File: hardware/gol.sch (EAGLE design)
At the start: 40 parts, among them U1 STM32F072CBT

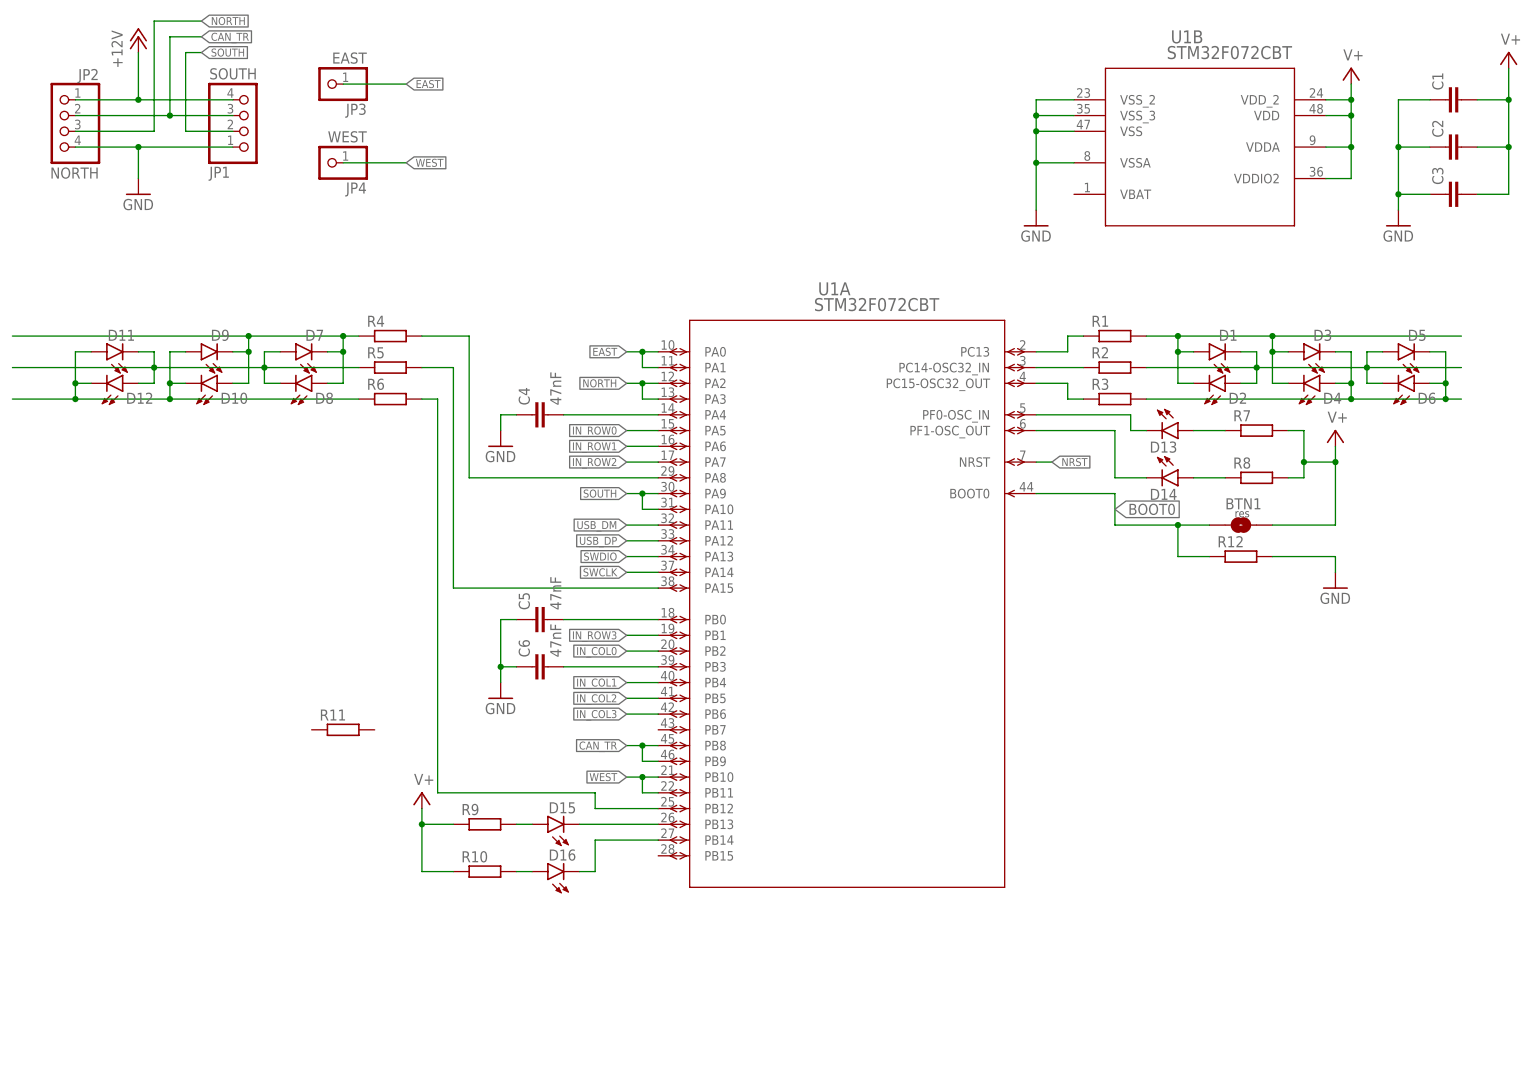
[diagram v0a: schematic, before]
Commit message: Adds buttons and LEDs, adds schematic for grids.
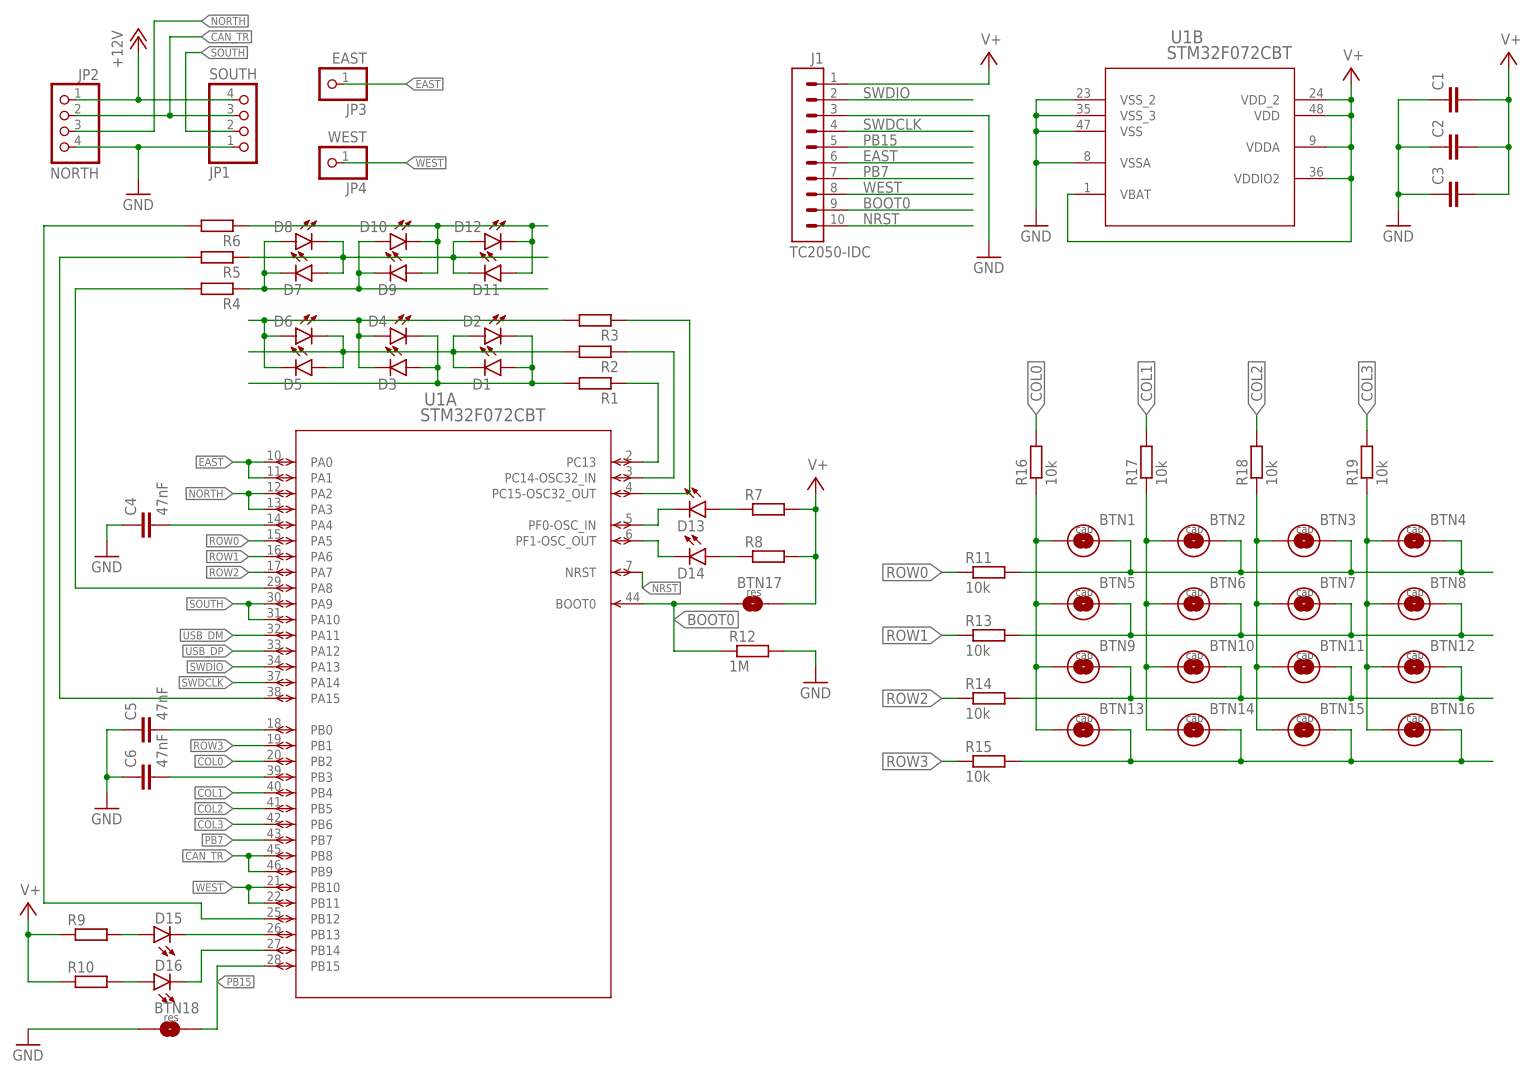
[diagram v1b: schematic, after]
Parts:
- added BTN10, BTN11, BTN12, BTN13, BTN14, BTN15, BTN16, BTN2, BTN3, BTN4, BTN5, BTN6, BTN7, BTN8, BTN9: BUTTON-CAP, parts:BUTTON-CAP
- added BTN17, BTN18: BUTTON-RES, parts:BUTTON-RES
- added J1: TC2050-IDC, tcs:TC2050-IDC
- added R13, R14, R15, R16, R17, R18, R19: 10k, rcl:R-EU_R0603
- BTN1: value BUTTON-RES -> BUTTON-CAP; device parts:BUTTON-RES -> parts:BUTTON-CAP
- R11: value (none) -> 10k; device rcl:R-EU_0207/10 -> rcl:R-EU_R0603
- R12: value (none) -> 1M
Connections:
- removed net SWCLK: U1A.PA14
- new net COL0: R16.2, U1A.PB2
- new net COL1: R17.2, U1A.PB4
- new net COL2: R18.2, U1A.PB5
- new net COL3: R19.2, U1A.PB6
- new net PB15: BTN18.2, J1.5, U1A.PB15
- new net PB7: J1.7, U1A.PB7
- new net ROW0: R11.1, U1A.PA5
- new net ROW1: R13.1, U1A.PA6
- new net ROW2: R14.1, U1A.PA7
- new net ROW3: R15.1, U1A.PB1
- new net SWDCLK: J1.4, U1A.PA14
- net BOOT0: now also BTN17.1, J1.9; no longer BTN1.1
- net EAST: now also J1.6
- net GND: now also BTN18.1, J1.3
- net IN_COL0: now also BTN1.1, BTN13.1, BTN5.1, BTN9.1, R16.1; no longer U1A.PB2
- net IN_COL1: now also BTN10.1, BTN14.1, BTN2.1, BTN6.1, R17.1; no longer U1A.PB4
- net IN_COL2: now also BTN11.1, BTN15.1, BTN3.1, BTN7.1, R18.1; no longer U1A.PB5
- net IN_COL3: now also BTN12.1, BTN16.1, BTN4.1, BTN8.1, R19.1; no longer U1A.PB6
- net IN_ROW0: now also BTN1.2, BTN2.2, BTN3.2, BTN4.2, R11.2; no longer U1A.PA5
- net IN_ROW1: now also BTN5.2, BTN6.2, BTN7.2, BTN8.2, R13.2; no longer U1A.PA6
- net IN_ROW2: now also BTN10.2, BTN11.2, BTN12.2, BTN9.2, R14.2; no longer U1A.PA7
- net IN_ROW3: now also BTN13.2, BTN14.2, BTN15.2, BTN16.2, R15.2; no longer U1A.PB1
- net NRST: now also J1.10
- net SWDIO: now also J1.2
- net V+: now also BTN17.2, J1.1, U1B.VBAT; no longer BTN1.2
- net WEST: now also J1.8
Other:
- moved on the sheet: C4, C5, C6, D1, D10, D11, D12, D13, D14, D15, D16, D2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

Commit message: Adds micro-usb connector and 5V to 3V3 voltage regulator.
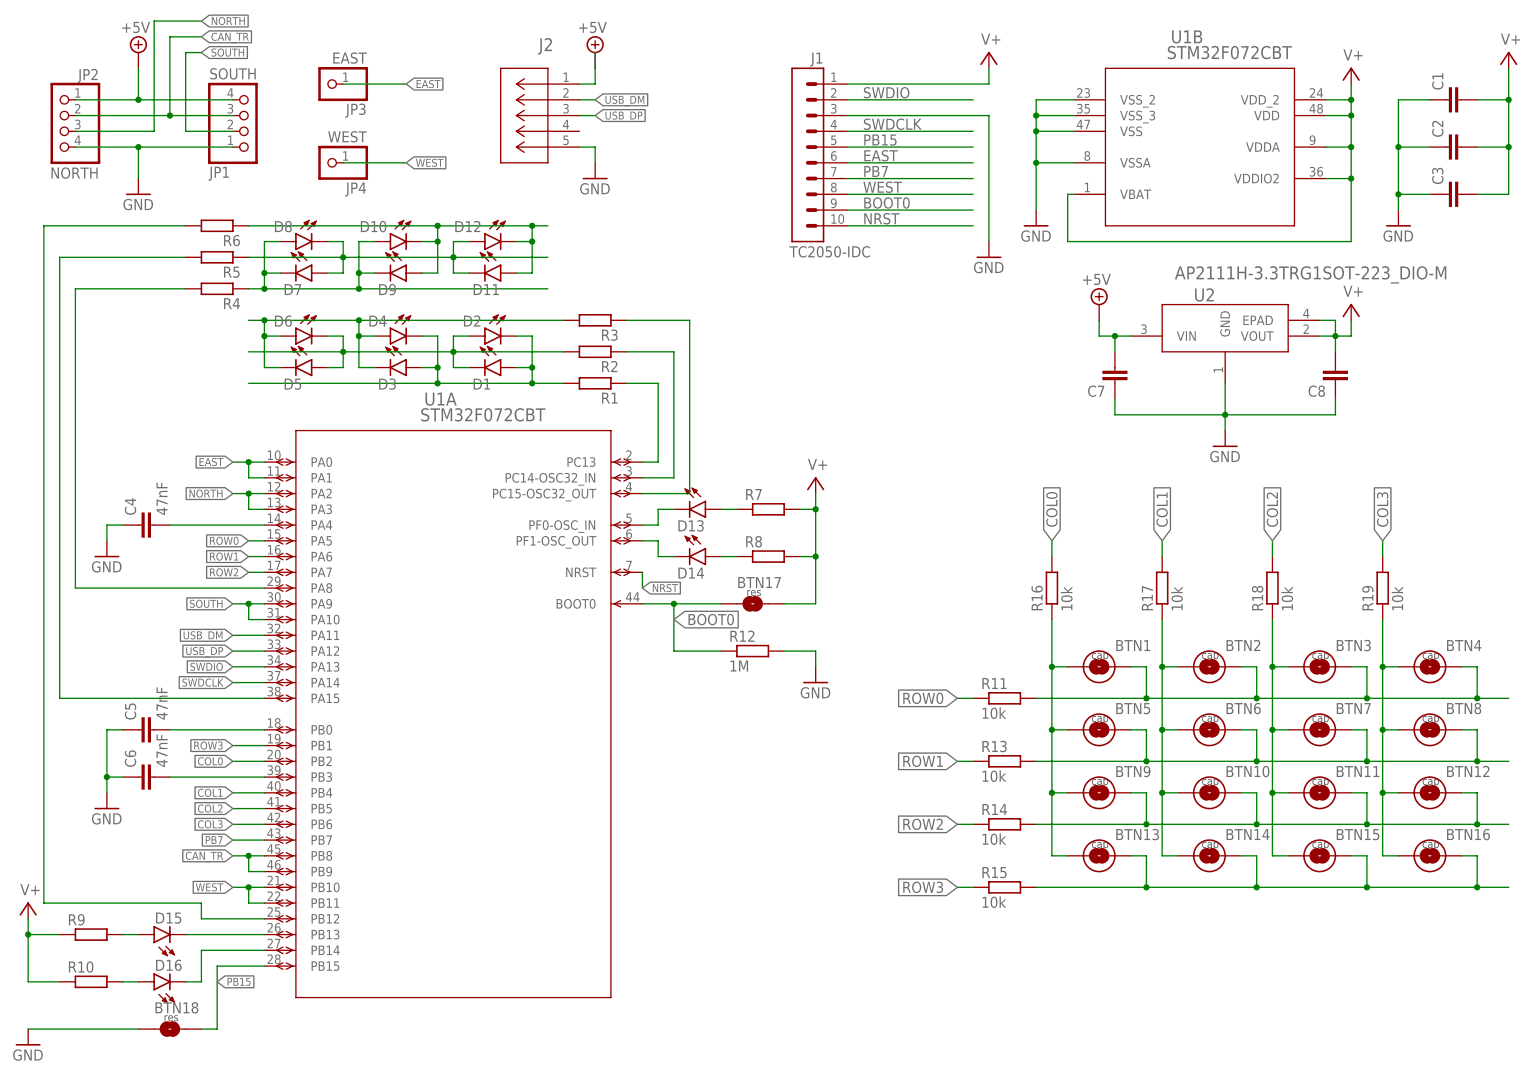
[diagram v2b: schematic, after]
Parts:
- added C7, C8: (no value), rcl:C-EUC0603
- added J2: 2057-MCR-B-S-RA-TSMT-NP-CS4-T/RCT-ND, parts:10118192-0002LFCONN_10118192-0002LF_AMP
- added U2: AP2111H-3.3TRG1SOT-223_DIO-M, parts:AP2111H-3.3TRG1SOT-223_DIO-M
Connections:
- removed net +12V: JP1.4, JP2.1
- new net +5V: C7.2, J2.1, JP1.4, JP2.1, U2.VIN
- net GND: now also C7.1, C8.1, J2.5, U2.GND
- net USB_DM: now also J2.2
- net USB_DP: now also J2.3
- net V+: now also C8.2, U2.EPAD, U2.VOUT
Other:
- moved on the sheet: BTN1, BTN10, BTN11, BTN12, BTN13, BTN14, BTN15, BTN16, BTN2, BTN3, BTN4, BTN5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

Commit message: Completes layout of top side components. Adds +12V grid horizontally.
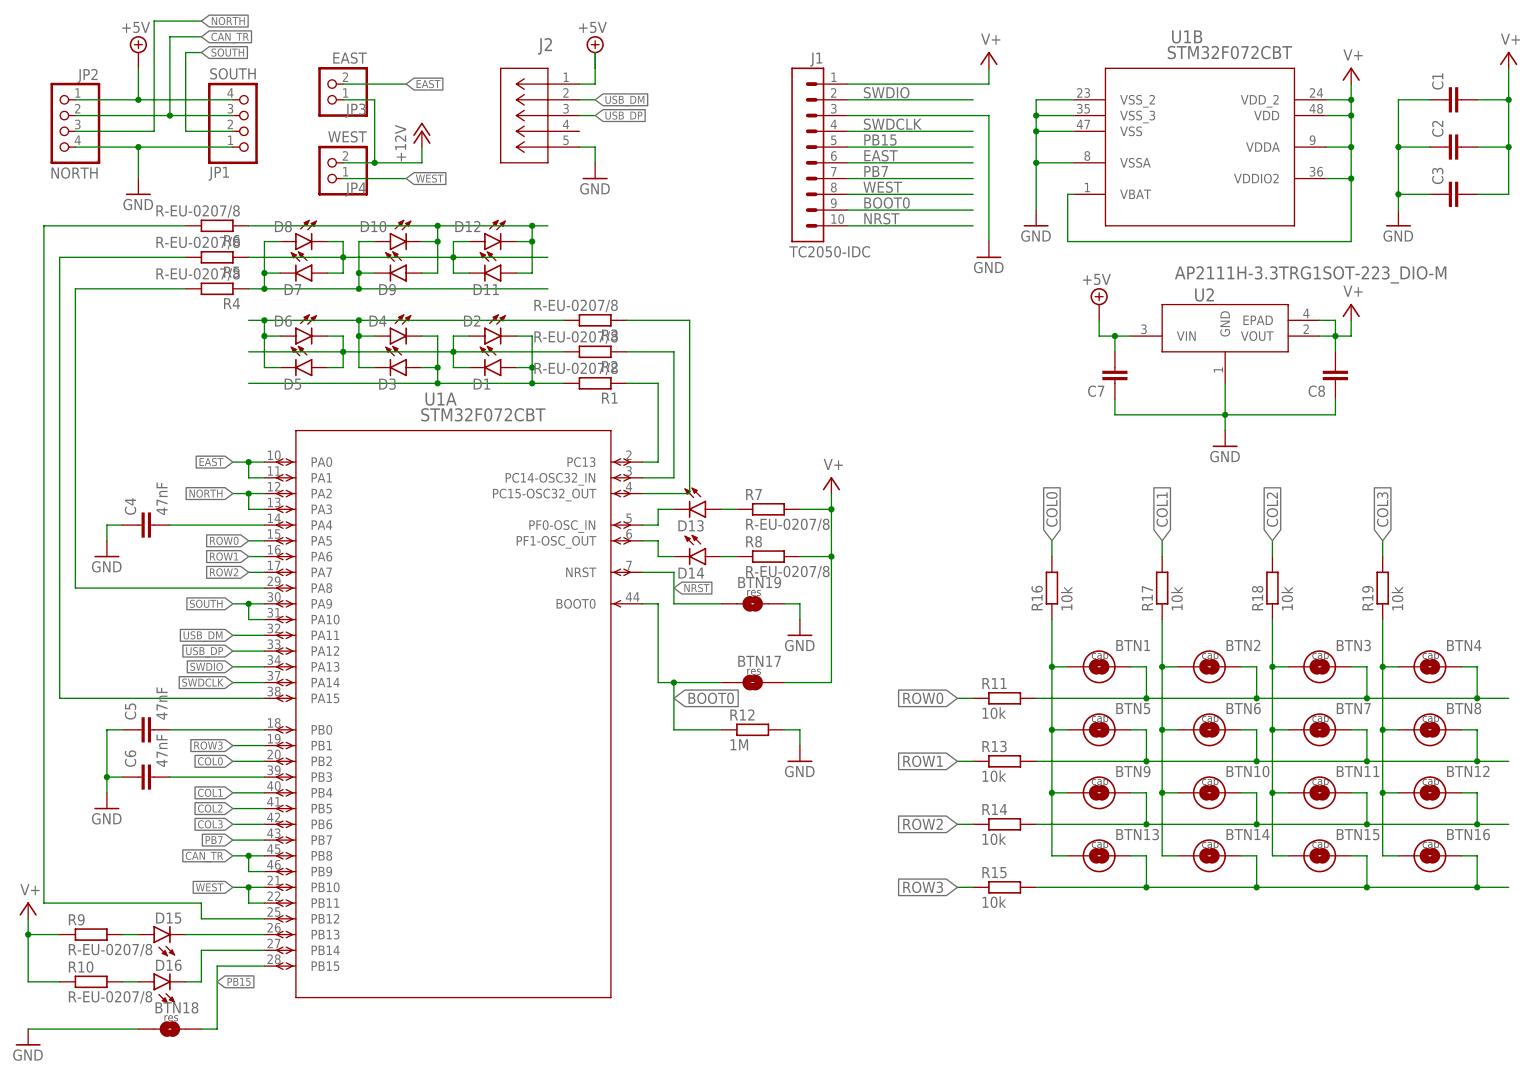
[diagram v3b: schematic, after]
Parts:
- added BTN19: RESET, parts:BUTTON-RES
- BTN17: value BUTTON-RES -> BOOT
- BTN18: value BUTTON-RES -> MENU
- JP3, JP4: device pinhead:PINHD-1X1 -> parts:PINHD-1X2
- R1, R10, R2, R3, R4, R5, R6, R7, R8, R9: value (none) -> R-EU-0207/8; device rcl:R-EU_0207/10 -> parts:R-EU-0207/8
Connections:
- new net +12V: JP3.1, JP4.2
- net EAST: now also JP3.2; no longer JP3.1
- net GND: now also BTN19.2
- net NRST: now also BTN19.1
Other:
- moved on the sheet: BTN17, R12

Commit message: Completes part of the layout and a small part of the routing around the MCU.
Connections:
- net N$10 renamed OUTB-L1
- net N$11 renamed OUTB-L2
- net N$12 renamed OUTB-L3
- net N$16 renamed OUTD13
- net N$17 renamed OUTD14
- net N$20 renamed OUTD15
- net N$21 renamed OUTD16
- net N$7 renamed OUTA-L2
- net N$8 renamed OUTA-L1
- net N$9 renamed OUTA-L3
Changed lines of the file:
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@@
 <instance part="R1" gate="G$1" x="99.06" y="114.3" smashed="yes" rot="R180">
 <attribute name="NAME" x="102.87" y="112.8014" size="1.778" layer="95" rot="R180"/>
-<attribute name="VALUE" x="102.87" y="117.602" size="1.778" layer="96" rot="R180"/>
 </instance>
 <instance part="R2" gate="G$1" x="99.06" y="119.38" smashed="yes" rot="R180">
 <attribute name="NAME" x="102.87" y="117.8814" size="1.778" layer="95" rot="R180"/>
-<attribute name="VALUE" x="102.87" y="122.682" size="1.778" layer="96" rot="R180"/>
 </instance>
 <instance part="R3" gate="G$1" x="99.06" y="124.46" smashed="yes" rot="R180">
 <attribute name="NAME" x="102.87" y="122.9614" size="1.778" layer="95" rot="R180"/>
-<attribute name="VALUE" x="102.87" y="127.762" size="1.778" layer="96" rot="R180"/>
 </instance>
 <instance part="R4" gate="G$1" x="38.1" y="129.54" smashed="yes" rot="R180">
 <attribute name="NAME" x="41.91" y="128.0414" size="1.778" layer="95" rot="R180"/>
-<attribute name="VALUE" x="41.91" y="132.842" size="1.778" layer="96" rot="R180"/>
 </instance>
 <instance part="R5" gate="G$1" x="38.1" y="134.62" smashed="yes" rot="R180">
 <attribute name="NAME" x="41.91" y="133.1214" size="1.778" layer="95" rot="R180"/>
-<attribute name="VALUE" x="41.91" y="137.922" size="1.778" layer="96" rot="R180"/>
 </instance>
 <instance part="R6" gate="G$1" x="38.1" y="139.7" smashed="yes" rot="R180">
 <attribute name="NAME" x="41.91" y="138.2014" size="1.778" layer="95" rot="R180"/>
-<attribute name="VALUE" x="41.91" y="143.002" size="1.778" layer="96" rot="R180"/>
 </instance>
 <instance part="R7" gate="G$1" x="127" y="93.98" smashed="yes">
@@
 <instance part="R9" gate="G$1" x="17.78" y="25.4" smashed="yes">
 <attribute name="NAME" x="13.97" y="26.8986" size="1.778" layer="95"/>
-<attribute name="VALUE" x="13.97" y="22.098" size="1.778" layer="96"/>
 </instance>
 <instance part="R10" gate="G$1" x="17.78" y="17.78" smashed="yes">
 <attribute name="NAME" x="13.97" y="19.2786" size="1.778" layer="95"/>
-<attribute name="VALUE" x="13.97" y="14.478" size="1.778" layer="96"/>
 </instance>
 <instance part="JP1" gate="A" x="43.18" y="157.48" smashed="yes" rot="MR180">
@@
 </segment>
 </net>
-<net name="N$7" class="0">
+<net name="OUTA-L2" class="0">
 <segment>
 <pinref part="R2" gate="G$1" pin="1"/>
@@
 </segment>
 </net>
-<net name="N$9" class="0">
+<net name="OUTA-L3" class="0">
 <segment>
 <pinref part="U1" gate="A" pin="PC15-OSC32_OUT"/>
@@
 </segment>
 </net>
-<net name="N$8" class="0">
+<net name="OUTA-L1" class="0">
 <segment>
 <pinref part="U1" gate="A" pin="PC13"/>
@@
 </segment>
 </net>
-<net name="N$10" class="0">
+<net name="OUTB-L1" class="0">
 <segment>
 <pinref part="U1" gate="A" pin="PA8"/>
@@
 </segment>
 </net>
-<net name="N$11" class="0">
+<net name="OUTB-L2" class="0">
 <segment>
 <pinref part="U1" gate="A" pin="PA15"/>
@@
 </segment>
 </net>
-<net name="N$12" class="0">
+<net name="OUTB-L3" class="0">
 <segment>
 <pinref part="R6" gate="G$1" pin="2"/>
@@
 </segment>
 </net>
-<net name="N$20" class="0">
+<net name="OUTD15" class="0">
 <segment>
 <pinref part="U1" gate="A" pin="PB13"/>
@@
 </segment>
 </net>
-<net name="N$21" class="0">
+<net name="OUTD16" class="0">
 <segment>
 <pinref part="U1" gate="A" pin="PB14"/>
@@
 </segment>
 </net>
-<net name="N$16" class="0">
+<net name="OUTD13" class="0">
 <segment>
 <pinref part="U1" gate="A" pin="PF0-OSC_IN"/>
@@
 </segment>
 </net>
-<net name="N$17" class="0">
+<net name="OUTD14" class="0">
 <segment>
 <pinref part="U1" gate="A" pin="PF1-OSC_OUT"/>

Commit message: more routing
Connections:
- net OUTB-L1: now also U1A.PA15; no longer U1A.PA8
- net OUTB-L2: now also U1A.PA8; no longer U1A.PA15
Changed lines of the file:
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@@
 <net name="OUTB-L1" class="0">
 <segment>
-<pinref part="U1" gate="A" pin="PA8"/>
-<wire x1="45.72" y1="81.28" x2="15.24" y2="81.28" width="0.1524" layer="91"/>
 <pinref part="R4" gate="G$1" pin="2"/>
-<wire x1="15.24" y1="81.28" x2="15.24" y2="129.54" width="0.1524" layer="91"/>
+<wire x1="15.24" y1="63.5" x2="15.24" y2="129.54" width="0.1524" layer="91"/>
 <wire x1="15.24" y1="129.54" x2="33.02" y2="129.54" width="0.1524" layer="91"/>
+<pinref part="U1" gate="A" pin="PA15"/>
+<wire x1="15.24" y1="63.5" x2="45.72" y2="63.5" width="0.1524" layer="91"/>
 </segment>
 </net>
 <net name="OUTB-L2" class="0">
 <segment>
-<pinref part="U1" gate="A" pin="PA15"/>
-<wire x1="45.72" y1="63.5" x2="12.7" y2="63.5" width="0.1524" layer="91"/>
 <pinref part="R5" gate="G$1" pin="2"/>
-<wire x1="12.7" y1="63.5" x2="12.7" y2="134.62" width="0.1524" layer="91"/>
+<wire x1="12.7" y1="81.28" x2="12.7" y2="134.62" width="0.1524" layer="91"/>
 <wire x1="12.7" y1="134.62" x2="33.02" y2="134.62" width="0.1524" layer="91"/>
+<pinref part="U1" gate="A" pin="PA8"/>
+<wire x1="12.7" y1="81.28" x2="45.72" y2="81.28" width="0.1524" layer="91"/>
 </segment>
 </net>
